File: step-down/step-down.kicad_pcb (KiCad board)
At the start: 2 copper layers, 10 x 14.2 mm, 16 parts, among them J1 Conn_01x01_Pin, J2 Conn_01x01_Pin, J4 Conn_01x01_Pin

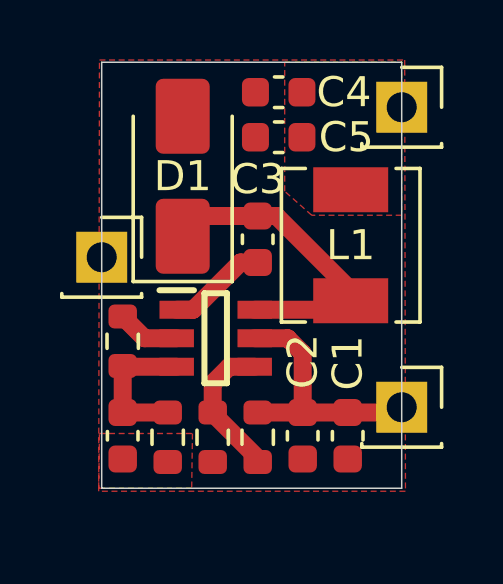
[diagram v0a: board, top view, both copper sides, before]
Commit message: moved EN logic to external control
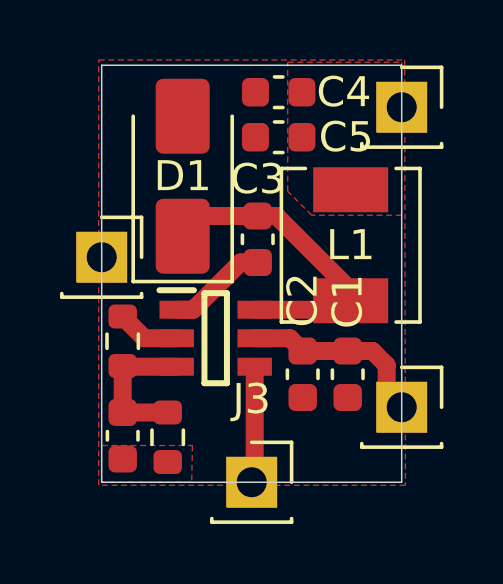
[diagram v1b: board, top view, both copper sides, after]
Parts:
- removed R1, R2: 10k, Resistor_SMD:R_0603_1608Metric
- added J3: Conn_01x01_Pin, Connector_PinSocket_2.54mm:PinSocket_1x01_P2.54mm_Vertical, F.Cu at (101.1, 91.9)
- moved C1 2.05 mm to (104.3, 88.3)
- moved C2 2.05 mm to (102.8, 88.3)
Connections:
- PS1 pad 4: Net-(PS1-EN) -> /EN
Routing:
- net Net-(PS1-EN): track 4.87 -> 0.00 mm
- net /EN: track 0.00 -> 3.89 mm
- net +BATT: track 8.65 -> 6.07 mm
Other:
- board size 10 x 14.2 mm -> 10 x 13.9 mm
